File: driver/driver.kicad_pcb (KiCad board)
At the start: 2 copper layers, 100 x 100 mm, 107 parts, among them J1 OUT_A, J2 OUT_B, J3 UART_DEBUG, J4 USB_B_Micro, J5 CH340E module, J6 1602 I2C LCD, J7 IN_VCC, J8 IN_GND, Q1 TPHR6503PL, Q2 TPHR6503PL, Q3 TPHR6503PL, Q4 TPHR6503PL, SW1 SW_Push, SW2 SW_Push, U1 MT3608, U10 PC817, U2 AMS1117-5.0, U3 AMS1117-3.3, U4 TC4427, U5 TC4427, U6 STM32F103C8Tx, U7 INA226, U8 MCP9804_MSOP, U9 PC817, Y1 8MHz

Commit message: driver: Continue layout
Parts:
- removed C7, C8: 1u, Capacitors_SMD:C_0603_HandSoldering
- removed R6: 10R .5W, Resistor_SMD:R_1206_3216Metric_Pad1.42x1.75mm_HandSolder
- C15: footprint Capacitors_SMD:C_0603_HandSoldering -> Capacitor_THT:CP_Radial_D10.0mm_P5.00mm
- C19, C2, C3: footprint Capacitor_THT:CP_Radial_D12.5mm_P5.00mm -> Capacitor_THT:CP_Radial_D10.0mm_P5.00mm
- C6: value 100u -> 100n; footprint Capacitor_THT:CP_Radial_D12.5mm_P5.00mm -> Capacitors_SMD:C_0603_HandSoldering
- moved R1 115.9 mm to (84.2, 70.7)
- moved R27 113.8 mm to (126.0, 65.0), turned to 180 degrees
- moved R18 113.5 mm to (148.0, 58.8), turned to 90 degrees
- moved R5 112.8 mm to (115.1, 66.1), turned to 270 degrees
- moved R24 111.6 mm to (135.0, 63.2), turned to 270 degrees
- moved R12 109.7 mm to (146.0, 58.8), turned to 90 degrees
- moved R3 108.5 mm to (110.9, 68.1), turned to 90 degrees
- moved R4 107.0 mm to (106.9, 72.0), turned to 90 degrees
- moved U1 106.7 mm to (97.3, 69.9), turned to 90 degrees
- moved R7 106.7 mm to (73.2, 82.0)
- moved R11 105.8 mm to (117.0, 62.0), turned to 90 degrees
- moved R17 105.5 mm to (119.1, 62.0), turned to 90 degrees
- moved R25 104.9 mm to (137.5, 63.2), turned to 90 degrees
- moved R2 104.6 mm to (107.7, 69.1)
- moved L1 104.4 mm to (91.0, 69.9), turned to 270 degrees
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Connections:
- C6 pad 1: Net-(C6-Pad1) -> +3V3
- R13 pad 2: Net-(D4-Pad2) -> Net-(D7-Pad2)
- R16 pad 2: Net-(D7-Pad2) -> Net-(D4-Pad2)
- R17 pad 2: Net-(D8-Pad2) -> Net-(D9-Pad2)
- R18 pad 2: Net-(D9-Pad2) -> Net-(D8-Pad2)
- U2 pad 3: Net-(C6-Pad1) -> Net-(C15-Pad1)
- U6 pad 15: /LED5 -> /LED2
- U6 pad 16: /LED6 -> /LED5
- U6 pad 20: /LED2 -> /LED6
- U8 pad 4: GND -> /GND_MEAS
- U8 pad 5: GND -> /GND_MEAS
- U8 pad 6: GND -> /GND_MEAS
- U8 pad 7: GND -> /GND_MEAS
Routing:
- net +3V3: track 0.00 -> 192.8 mm, vias 0 -> 1
- net Net-(D4-Pad2): track 0.00 -> 114.1 mm, vias 0 -> 2
- net Net-(D7-Pad2): track 0.00 -> 111.6 mm
- net GND: track 18.8 -> 128.8 mm, vias 0 -> 41
- net /VIN: track 0.00 -> 103.7 mm, vias 94 -> 95
- net Net-(D5-Pad2): track 0.00 -> 103.1 mm, vias 0 -> 2
- net +VSW: track 0.00 -> 103.1 mm, vias 0 -> 2
- net Net-(D6-Pad2): track 0.00 -> 100.0 mm, vias 0 -> 2
- net /SDA_INA: track 0.00 -> 87.6 mm, vias 0 -> 1
- net /SCL_INA: track 0.00 -> 84.8 mm
- net /DRV2F: track 0.00 -> 73.8 mm, vias 0 -> 2
- net /DRV4F: track 0.00 -> 60.9 mm, vias 0 -> 2
- net /VIN_MON: track 0.00 -> 47.4 mm
- net +5V: track 0.00 -> 33.8 mm
- net /DRV3F: track 0.00 -> 33.6 mm, vias 0 -> 2
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- added copper zone on B.Cu, net /ISO_GND
- added copper zone on F.Cu, net /ISO_GND
- added copper zone on B.Cu, net GND
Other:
- rule trace_min: 0.2 -> 0.15

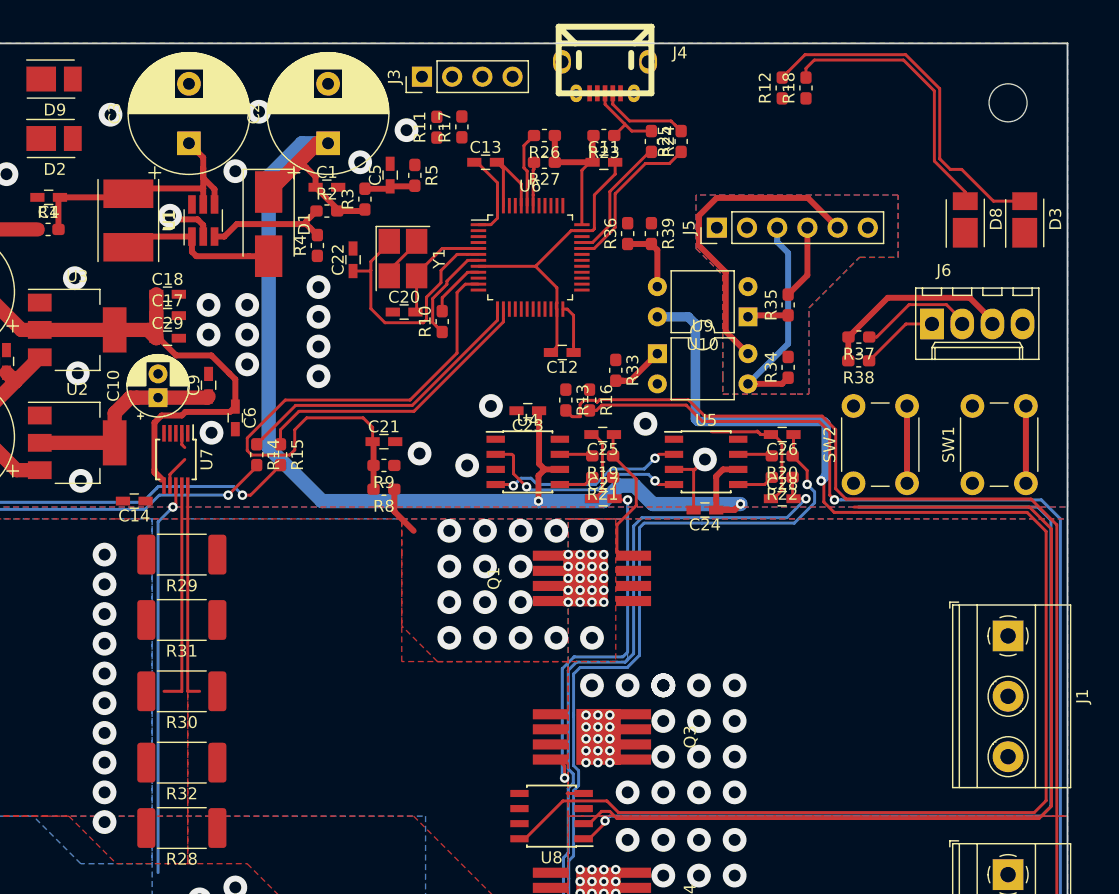
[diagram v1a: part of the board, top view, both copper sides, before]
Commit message: driver: Initial layout almost done
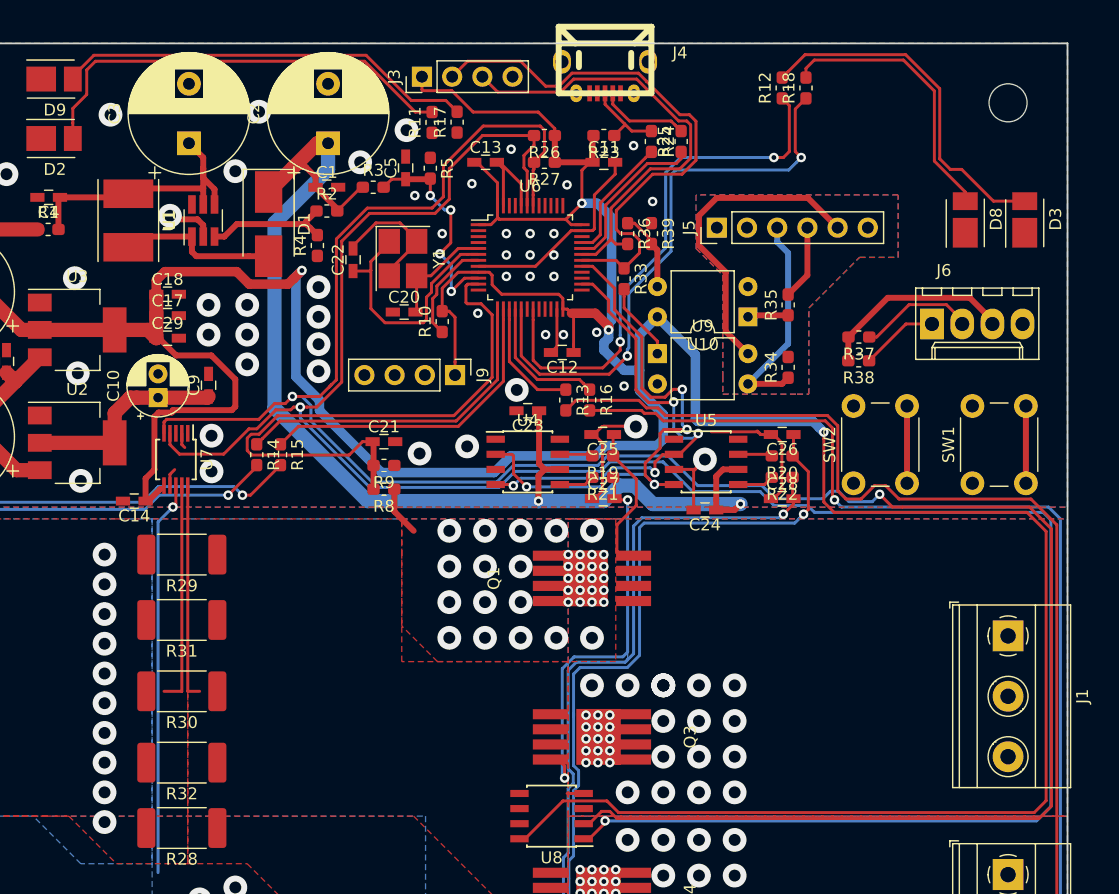
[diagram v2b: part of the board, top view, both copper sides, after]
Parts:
- removed C6: 100n, Capacitors_SMD:C_0603_HandSoldering
- added J9: SWD, Pin_Headers:Pin_Header_Straight_1x04_Pitch2.54mm, F.Cu at (118.5, 82.9)
- moved R33 7.73 mm to (132.7, 74.8)
- moved R5 1.43 mm to (116.4, 65.5)
- moved C5 1.43 mm to (114.3, 65.5)
- moved R3 1.22 mm to (111.6, 67.1), turned to 0 degrees
- moved R11 0.57 mm to (116.5, 61.6)
- moved R17 0.57 mm to (118.7, 61.6)
- turned R36 to 270 degrees
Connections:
- U6 pad 26: /DRV_B -> /CTRL_B
- U6 pad 29: /DRV_A -> /CTRL_A
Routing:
- net +3V3: track 192.8 -> 324.7 mm, vias 1 -> 4
- net /SCL_INA: track 84.8 -> 194.7 mm, vias 0 -> 2
- net /SDA_INA: track 87.6 -> 191.8 mm, vias 1 -> 2
- net /LED7: track 0.00 -> 48.0 mm, vias 0 -> 2
- net /UART_TX: track 0.00 -> 46.4 mm
- net /LED1: track 0.00 -> 44.9 mm, vias 0 -> 2
- net /UART_RX: track 0.00 -> 38.5 mm
- net Net-(D2-Pad2): track 0.00 -> 37.4 mm
- net Net-(D9-Pad2): track 0.00 -> 35.3 mm
- net /CTRL_A: track 18.0 -> 45.7 mm, vias 2 -> 4
- net /CTRL_B: track 16.6 -> 39.6 mm, vias 2 -> 4
- net /VBOOT_MON: track 4.30 -> 18.2 mm, vias 0 -> 4
- net /LED5: track 0.00 -> 11.4 mm
- net /LED2: track 0.00 -> 10.1 mm
- net GND: track 128.8 -> 134.1 mm, vias 41 -> 63
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
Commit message: driver: Finish initial routing
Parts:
- moved R12 9.61 mm to (153.7, 64.5), turned to 0 degrees
- moved C21 7.87 mm to (105.5, 92.1), turned to 90 degrees
- moved R18 6.31 mm to (149.4, 64.9), turned to 0 degrees
- moved R9 5.25 mm to (107.5, 92.1), turned to 270 degrees
- moved R14 4.62 mm to (98.9, 93.2), turned to 180 degrees
- moved R15 3.79 mm to (102.6, 93.2), turned to 0 degrees
- moved R8 3.03 mm to (109.5, 92.1), turned to 270 degrees
- moved R16 2.19 mm to (131.8, 85.9), turned to 0 degrees
- moved R24 1.30 mm to (135.0, 62.0)
- moved R25 1.30 mm to (137.5, 62.0)
- moved R13 1.03 mm to (128.3, 85.9), turned to 0 degrees
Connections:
- U6 pad 18: /LED0 -> Net-(U6-Pad18)
- U6 pad 2: Net-(U6-Pad2) -> /LED6
- U6 pad 20: /LED6 -> Net-(U6-Pad20)
- U6 pad 3: Net-(U6-Pad3) -> /LED0
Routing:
- net /SCL_LCD: track 6.57 -> 96.3 mm, vias 0 -> 2
- net /SDA_LCD: track 9.79 -> 95.4 mm, vias 0 -> 2
- net /SW1: track 6.50 -> 84.8 mm, vias 0 -> 2
- net +5V: track 33.8 -> 107.2 mm, vias 0 -> 4
- net /SW0: track 6.50 -> 77.4 mm, vias 0 -> 2
- net /UART_TX: track 46.4 -> 103.7 mm
- net +3V3: track 324.7 -> 306.7 mm, vias 4 -> 6
- net Net-(D3-Pad2): track 29.8 -> 13.3 mm
- net GND: track 134.1 -> 149.1 mm, vias 63 -> 65
- net /LED0: track 0.00 -> 11.0 mm, vias 0 -> 2
- net Net-(D8-Pad2): track 23.3 -> 12.7 mm
- net /LED6: track 0.00 -> 9.79 mm, vias 0 -> 2
- net /VIN: track 103.7 -> 111.0 mm
- net /LED4: track 27.0 -> 34.1 mm
- net /LED3: track 28.4 -> 33.8 mm
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
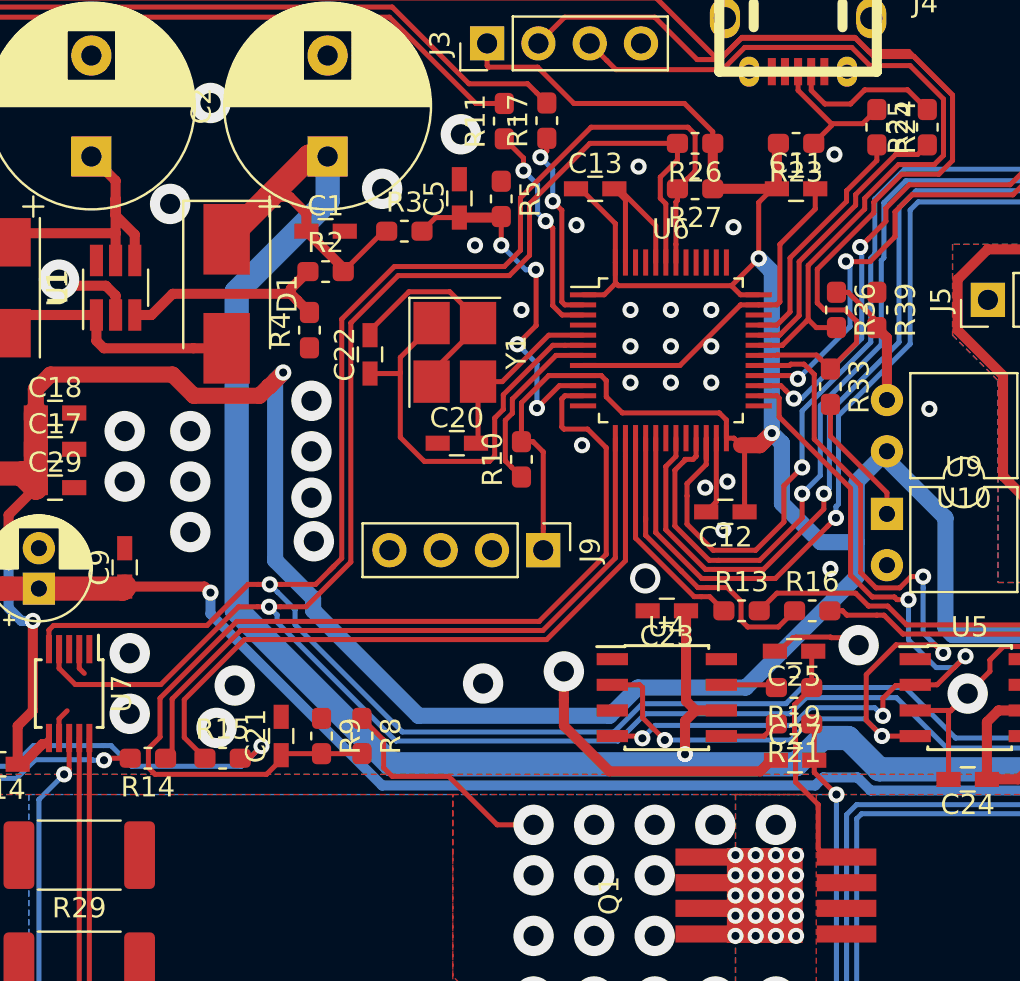
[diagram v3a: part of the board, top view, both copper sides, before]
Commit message: driver: initial DRC done
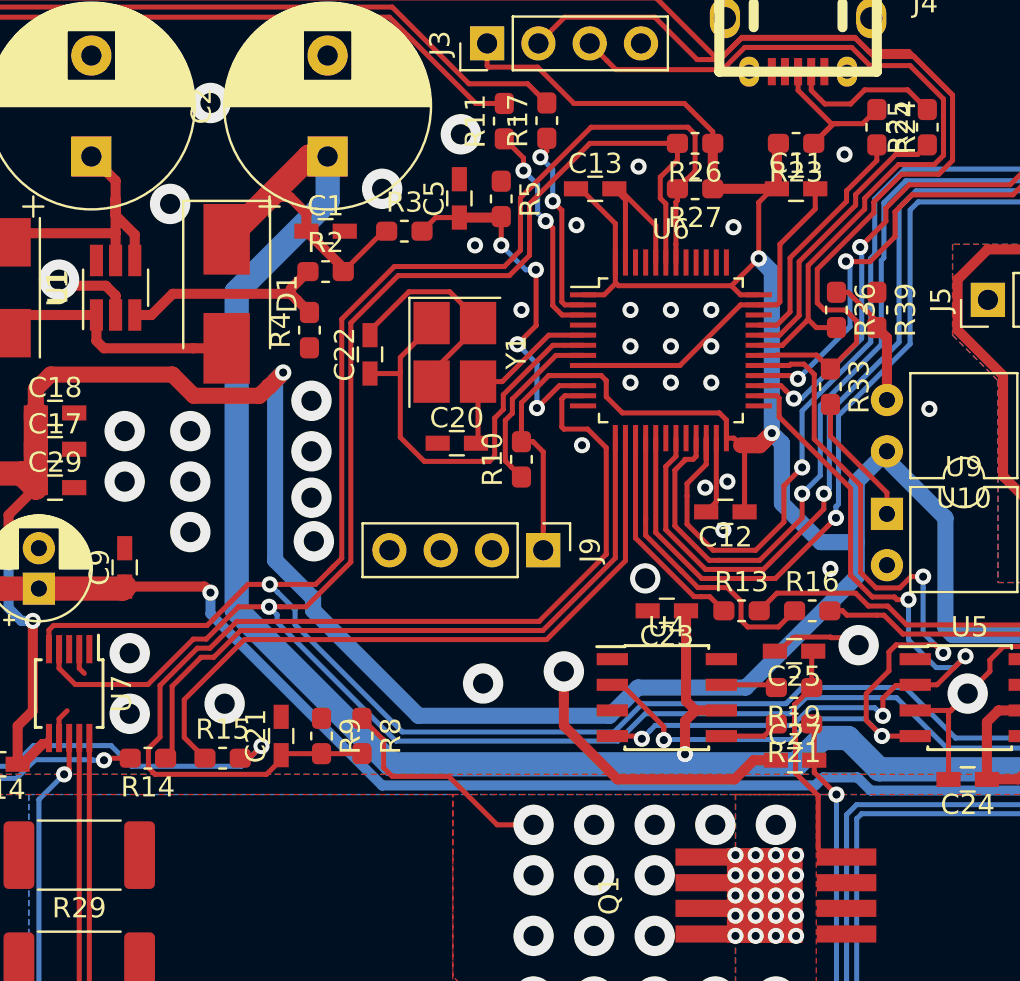
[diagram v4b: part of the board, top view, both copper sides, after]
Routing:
- net Net-(J4-Pad3): track 7.14 -> 8.76 mm
- net GND: track 149.1 -> 149.4 mm, vias 65 -> 64

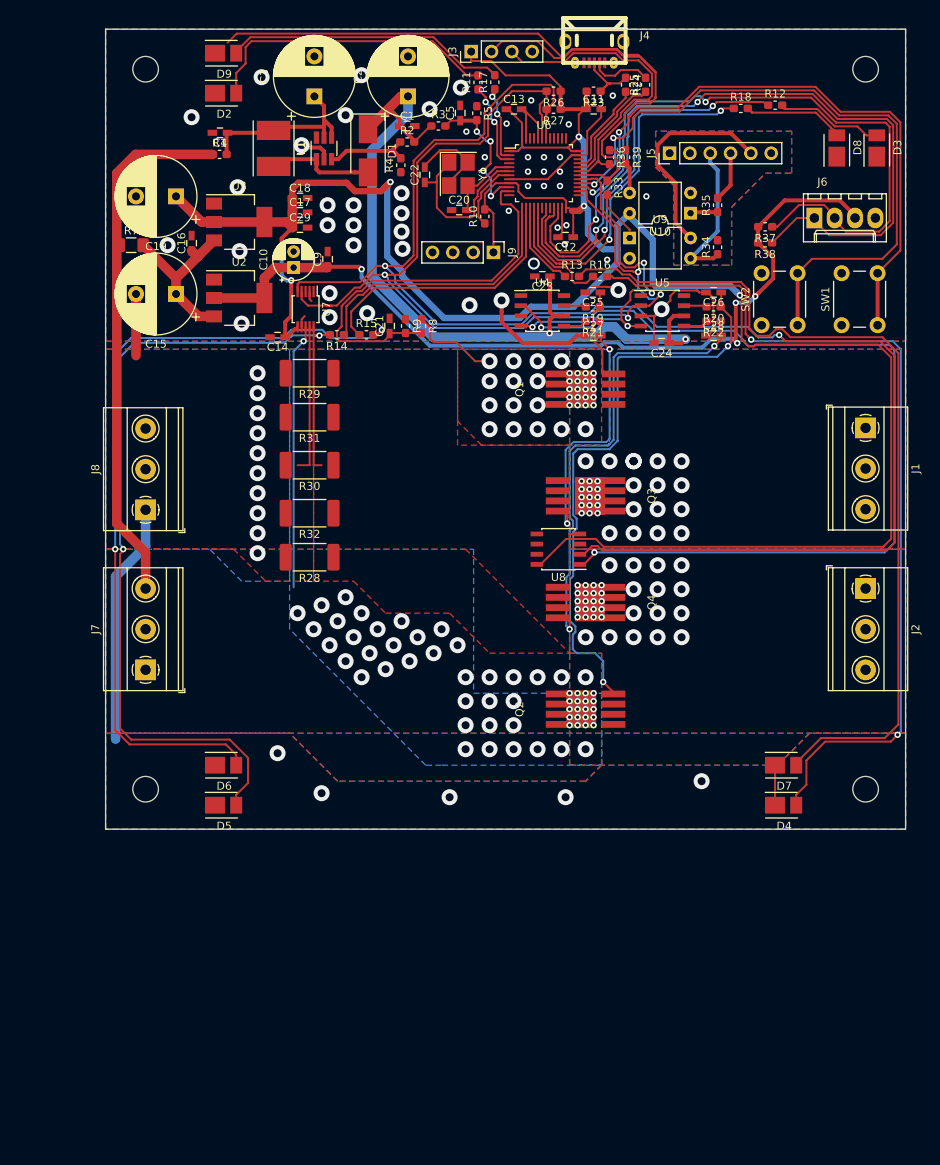
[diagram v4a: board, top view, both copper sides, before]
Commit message: driver: Fixup SWD header, swap driver outputs for VSW split, finish silk
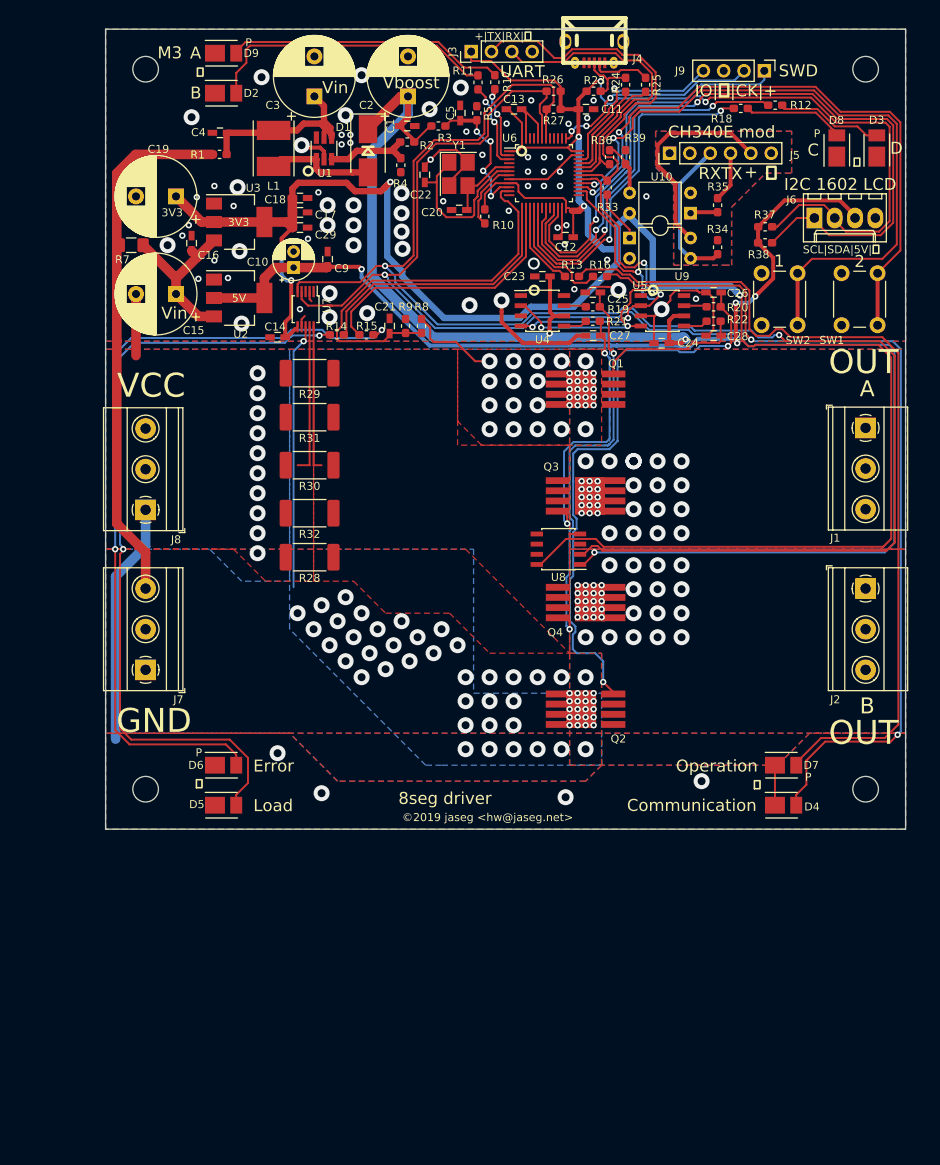
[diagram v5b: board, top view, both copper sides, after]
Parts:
- moved J9 40.8 mm to (152.3, 60.2)
- moved C11 0.95 mm to (130.1, 65.0)
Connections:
- Q1 pad 2: /DRV1F -> /DRV4F
- Q4 pad 2: /DRV4F -> /DRV1F
- U6 pad 34: Net-(U6-Pad34) -> /SWDIO
- U6 pad 37: Net-(U6-Pad37) -> /SWCLK
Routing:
- net /UART_TX: track 103.7 -> 46.6 mm
- net /DRV4F: track 58.8 -> 18.5 mm, vias 2 -> 0
- net /DRV1F: track 12.2 -> 51.0 mm, vias 0 -> 2
- net /SWCLK: track 0.00 -> 26.7 mm, vias 0 -> 3
- net /SWDIO: track 0.00 -> 23.9 mm, vias 0 -> 1
- net +3V3: track 306.7 -> 327.3 mm, vias 6 -> 7
- net GND: track 149.4 -> 142.0 mm, vias 64 -> 83
- net Net-(C3-Pad1): track 24.2 -> 28.9 mm
- net Net-(J4-Pad3): track 8.76 -> 7.59 mm
- net /VIN_MON: track 50.8 -> 49.9 mm
- net /CTRL_A: track 46.8 -> 46.1 mm
- net Net-(D2-Pad2): track 37.4 -> 36.7 mm
- net /SW1: track 84.8 -> 85.4 mm
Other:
- board text added: "+"
- board text added: "+|TX|RX|⏚"
- board text added: "1"
- board text added: "2"
- board text added: "3V3"
- board text added: "5V"
- board text added: "8seg driver"
- board text added: "A"
- board text added: "B"
- board text added: "C"
- board text added: "CH340E mod"
- board text added: "Communication"
- board text added: "D"
- board text added: "Error"
- board text added: "GND"
- board text added: "I2C 1602 LCD"
- board text added: "IO|⏚|CK|+"
- board text added: "Load"
- board text added: "M3"
- board text added: "OUT"
- board text added: "Operation"
- board text added: "P"
- board text added: "RX"
- board text added: "SCL|SDA|5V|⏚"
- board text added: "SWD"
- board text added: "TX"
- board text added: "UART"
- board text added: "VCC"
- board text added: "Vboost"
- board text added: "Vin"
- board text added: "©2019 jaseg <hw@jaseg.net>"
- board text added: "⏚"
